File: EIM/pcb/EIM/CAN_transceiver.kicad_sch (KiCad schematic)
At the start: 5 parts, among them U3 SN65HVD233

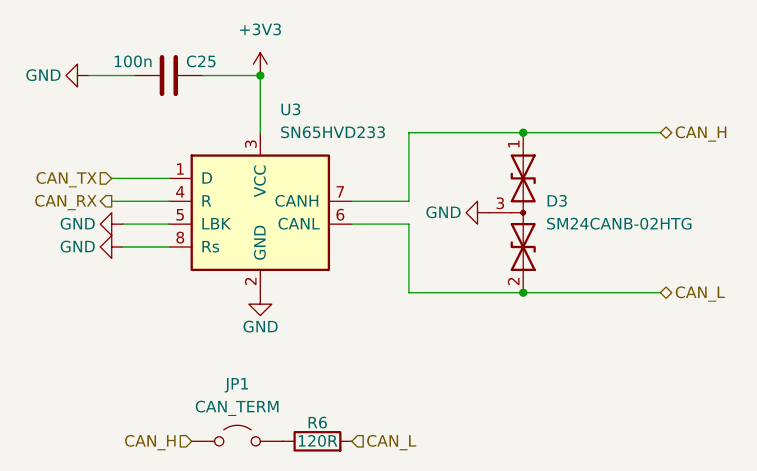
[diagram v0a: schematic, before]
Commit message: added Arjun's comments, assigned some MCU pins
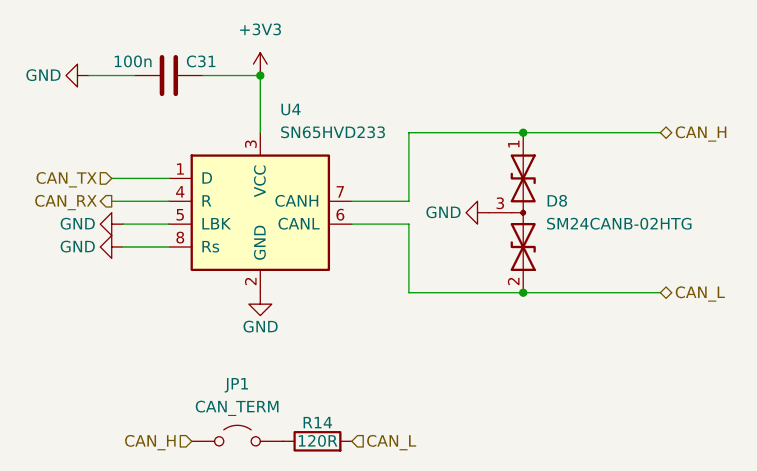
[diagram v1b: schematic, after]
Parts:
- renumbered C25 to C31, D3 to D8, R6 to R14, U3 to U4
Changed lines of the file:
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@@
 		(dnp no)
 		(fields_autoplaced yes)
-		(property "Reference" "#PWR034"
+		(property "Reference" "#PWR071"
 			(at 146.05 83.82 0)
 			(effects
@@
 			(project "EIM"
 				(path "/2e0b3b3d-5537-41dc-9fad-4fb33afdbfad/69c642dd-37c7-4978-9805-ffb4d10279e9"
-					(reference "#PWR034")
-					(unit 1)
-				)
-				(path "/2e0b3b3d-5537-41dc-9fad-4fb33afdbfad/adcbb2f8-dbde-4949-a46c-bc524f70d203"
-					(reference "#PWR041")
+					(reference "#PWR071")
+					(unit 1)
+				)
+				(path "/2e0b3b3d-5537-41dc-9fad-4fb33afdbfad/adcbb2f8-dbde-4949-a46c-bc524f70d203"
+					(reference "#PWR077")
 					(unit 1)
 				)
@@
 		(on_board yes)
 		(dnp no)
-		(property "Reference" "R6"
+		(property "Reference" "R14"
 			(at 152.4 118.618 90)
 			(effects
@@
 			(project "EIM"
 				(path "/2e0b3b3d-5537-41dc-9fad-4fb33afdbfad/69c642dd-37c7-4978-9805-ffb4d10279e9"
-					(reference "R6")
-					(unit 1)
-				)
-				(path "/2e0b3b3d-5537-41dc-9fad-4fb33afdbfad/adcbb2f8-dbde-4949-a46c-bc524f70d203"
-					(reference "R7")
+					(reference "R14")
+					(unit 1)
+				)
+				(path "/2e0b3b3d-5537-41dc-9fad-4fb33afdbfad/adcbb2f8-dbde-4949-a46c-bc524f70d203"
+					(reference "R15")
 					(unit 1)
 				)
@@
 		(on_board yes)
 		(dnp no)
-		(property "Reference" "#PWR048"
+		(property "Reference" "#PWR073"
 			(at 165.1 95.25 0)
 			(effects
@@
 			(project "EIM"
 				(path "/2e0b3b3d-5537-41dc-9fad-4fb33afdbfad/69c642dd-37c7-4978-9805-ffb4d10279e9"
-					(reference "#PWR048")
-					(unit 1)
-				)
-				(path "/2e0b3b3d-5537-41dc-9fad-4fb33afdbfad/adcbb2f8-dbde-4949-a46c-bc524f70d203"
-					(reference "#PWR049")
+					(reference "#PWR073")
+					(unit 1)
+				)
+				(path "/2e0b3b3d-5537-41dc-9fad-4fb33afdbfad/adcbb2f8-dbde-4949-a46c-bc524f70d203"
+					(reference "#PWR079")
 					(unit 1)
 				)
@@
 		(dnp no)
 		(fields_autoplaced yes)
-		(property "Reference" "D3"
+		(property "Reference" "D8"
 			(at 177.8 93.9799 90)
 			(effects
@@
 			(project "EIM"
 				(path "/2e0b3b3d-5537-41dc-9fad-4fb33afdbfad/69c642dd-37c7-4978-9805-ffb4d10279e9"
-					(reference "D3")
-					(unit 1)
-				)
-				(path "/2e0b3b3d-5537-41dc-9fad-4fb33afdbfad/adcbb2f8-dbde-4949-a46c-bc524f70d203"
-					(reference "D4")
+					(reference "D8")
+					(unit 1)
+				)
+				(path "/2e0b3b3d-5537-41dc-9fad-4fb33afdbfad/adcbb2f8-dbde-4949-a46c-bc524f70d203"
+					(reference "D9")
 					(unit 1)
 				)
@@
 		(on_board yes)
 		(dnp no)
-		(property "Reference" "C25"
+		(property "Reference" "C31"
 			(at 141.224 78.486 90)
 			(effects
@@
 			(project "EIM"
 				(path "/2e0b3b3d-5537-41dc-9fad-4fb33afdbfad/69c642dd-37c7-4978-9805-ffb4d10279e9"
-					(reference "C25")
-					(unit 1)
-				)
-				(path "/2e0b3b3d-5537-41dc-9fad-4fb33afdbfad/adcbb2f8-dbde-4949-a46c-bc524f70d203"
-					(reference "C26")
+					(reference "C31")
+					(unit 1)
+				)
+				(path "/2e0b3b3d-5537-41dc-9fad-4fb33afdbfad/adcbb2f8-dbde-4949-a46c-bc524f70d203"
+					(reference "C32")
 					(unit 1)
 				)
@@
 		(on_board yes)
 		(dnp no)
-		(property "Reference" "#PWR035"
+		(property "Reference" "#PWR072"
 			(at 146.05 110.49 0)
 			(effects
@@
 			(project "EIM"
 				(path "/2e0b3b3d-5537-41dc-9fad-4fb33afdbfad/69c642dd-37c7-4978-9805-ffb4d10279e9"
-					(reference "#PWR035")
-					(unit 1)
-				)
-				(path "/2e0b3b3d-5537-41dc-9fad-4fb33afdbfad/adcbb2f8-dbde-4949-a46c-bc524f70d203"
-					(reference "#PWR042")
+					(reference "#PWR072")
+					(unit 1)
+				)
+				(path "/2e0b3b3d-5537-41dc-9fad-4fb33afdbfad/adcbb2f8-dbde-4949-a46c-bc524f70d203"
+					(reference "#PWR078")
 					(unit 1)
 				)
@@
 		(on_board yes)
 		(dnp no)
-		(property "Reference" "#PWR036"
+		(property "Reference" "#PWR069"
 			(at 124.46 96.52 0)
 			(effects
@@
 			(project "EIM"
 				(path "/2e0b3b3d-5537-41dc-9fad-4fb33afdbfad/69c642dd-37c7-4978-9805-ffb4d10279e9"
-					(reference "#PWR036")
-					(unit 1)
-				)
-				(path "/2e0b3b3d-5537-41dc-9fad-4fb33afdbfad/adcbb2f8-dbde-4949-a46c-bc524f70d203"
-					(reference "#PWR039")
+					(reference "#PWR069")
+					(unit 1)
+				)
+				(path "/2e0b3b3d-5537-41dc-9fad-4fb33afdbfad/adcbb2f8-dbde-4949-a46c-bc524f70d203"
+					(reference "#PWR075")
 					(unit 1)
 				)
@@
 		(on_board yes)
 		(dnp no)
-		(property "Reference" "#PWR037"
+		(property "Reference" "#PWR070"
 			(at 124.46 99.06 0)
 			(effects
@@
 			(project "EIM"
 				(path "/2e0b3b3d-5537-41dc-9fad-4fb33afdbfad/69c642dd-37c7-4978-9805-ffb4d10279e9"
-					(reference "#PWR037")
-					(unit 1)
-				)
-				(path "/2e0b3b3d-5537-41dc-9fad-4fb33afdbfad/adcbb2f8-dbde-4949-a46c-bc524f70d203"
-					(reference "#PWR040")
+					(reference "#PWR070")
+					(unit 1)
+				)
+				(path "/2e0b3b3d-5537-41dc-9fad-4fb33afdbfad/adcbb2f8-dbde-4949-a46c-bc524f70d203"
+					(reference "#PWR076")
 					(unit 1)
 				)
@@
 		(on_board yes)
 		(dnp no)
-		(property "Reference" "#PWR033"
+		(property "Reference" "#PWR068"
 			(at 120.65 80.01 0)
 			(effects
@@
 			(project "EIM"
 				(path "/2e0b3b3d-5537-41dc-9fad-4fb33afdbfad/69c642dd-37c7-4978-9805-ffb4d10279e9"
-					(reference "#PWR033")
-					(unit 1)
-				)
-				(path "/2e0b3b3d-5537-41dc-9fad-4fb33afdbfad/adcbb2f8-dbde-4949-a46c-bc524f70d203"
-					(reference "#PWR038")
+					(reference "#PWR068")
+					(unit 1)
+				)
+				(path "/2e0b3b3d-5537-41dc-9fad-4fb33afdbfad/adcbb2f8-dbde-4949-a46c-bc524f70d203"
+					(reference "#PWR074")
 					(unit 1)
 				)
@@
 		(dnp no)
 		(fields_autoplaced yes)
-		(property "Reference" "U3"
+		(property "Reference" "U4"
 			(at 148.2441 83.82 0)
 			(effects
@@
 			(project "EIM"
 				(path "/2e0b3b3d-5537-41dc-9fad-4fb33afdbfad/69c642dd-37c7-4978-9805-ffb4d10279e9"
-					(reference "U3")
-					(unit 1)
-				)
-				(path "/2e0b3b3d-5537-41dc-9fad-4fb33afdbfad/adcbb2f8-dbde-4949-a46c-bc524f70d203"
 					(reference "U4")
 					(unit 1)
 				)
+				(path "/2e0b3b3d-5537-41dc-9fad-4fb33afdbfad/adcbb2f8-dbde-4949-a46c-bc524f70d203"
+					(reference "U5")
+					(unit 1)
+				)

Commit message: Layout 75% done, before 8V bus deletion
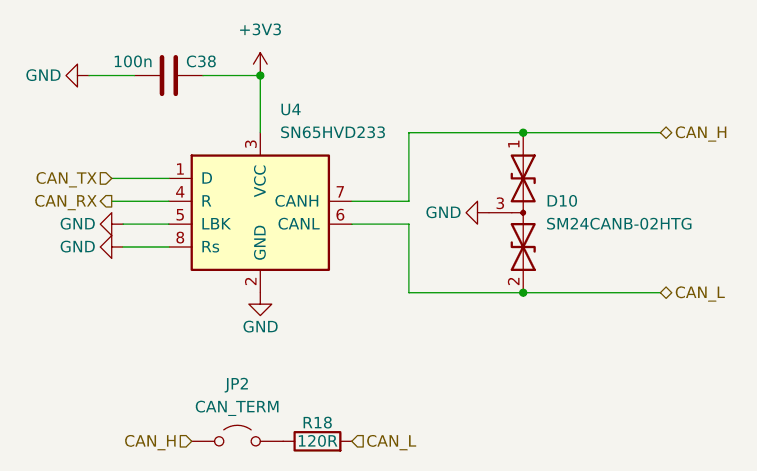
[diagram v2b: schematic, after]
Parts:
- renumbered C31 to C38, D8 to D10, JP1 to JP2, R14 to R18
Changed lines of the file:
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@@
 		(dnp no)
 		(fields_autoplaced yes)
-		(property "Reference" "#PWR071"
+		(property "Reference" "#PWR080"
 			(at 146.05 83.82 0)
 			(effects
@@
 			(project "EIM"
 				(path "/2e0b3b3d-5537-41dc-9fad-4fb33afdbfad/69c642dd-37c7-4978-9805-ffb4d10279e9"
-					(reference "#PWR071")
-					(unit 1)
-				)
-				(path "/2e0b3b3d-5537-41dc-9fad-4fb33afdbfad/adcbb2f8-dbde-4949-a46c-bc524f70d203"
-					(reference "#PWR077")
+					(reference "#PWR080")
+					(unit 1)
+				)
+				(path "/2e0b3b3d-5537-41dc-9fad-4fb33afdbfad/adcbb2f8-dbde-4949-a46c-bc524f70d203"
+					(reference "#PWR086")
 					(unit 1)
 				)
@@
 		(dnp no)
 		(fields_autoplaced yes)
-		(property "Reference" "JP1"
+		(property "Reference" "JP2"
 			(at 143.51 114.3 0)
 			(effects
@@
 			(project "EIM"
 				(path "/2e0b3b3d-5537-41dc-9fad-4fb33afdbfad/69c642dd-37c7-4978-9805-ffb4d10279e9"
-					(reference "JP1")
-					(unit 1)
-				)
-				(path "/2e0b3b3d-5537-41dc-9fad-4fb33afdbfad/adcbb2f8-dbde-4949-a46c-bc524f70d203"
 					(reference "JP2")
+					(unit 1)
+				)
+				(path "/2e0b3b3d-5537-41dc-9fad-4fb33afdbfad/adcbb2f8-dbde-4949-a46c-bc524f70d203"
+					(reference "JP3")
 					(unit 1)
 				)
@@
 		(on_board yes)
 		(dnp no)
-		(property "Reference" "R14"
+		(property "Reference" "R18"
 			(at 152.4 118.618 90)
 			(effects
@@
 			(project "EIM"
 				(path "/2e0b3b3d-5537-41dc-9fad-4fb33afdbfad/69c642dd-37c7-4978-9805-ffb4d10279e9"
-					(reference "R14")
-					(unit 1)
-				)
-				(path "/2e0b3b3d-5537-41dc-9fad-4fb33afdbfad/adcbb2f8-dbde-4949-a46c-bc524f70d203"
-					(reference "R15")
+					(reference "R18")
+					(unit 1)
+				)
+				(path "/2e0b3b3d-5537-41dc-9fad-4fb33afdbfad/adcbb2f8-dbde-4949-a46c-bc524f70d203"
+					(reference "R19")
 					(unit 1)
 				)
@@
 		(on_board yes)
 		(dnp no)
-		(property "Reference" "#PWR073"
+		(property "Reference" "#PWR082"
 			(at 165.1 95.25 0)
 			(effects
@@
 			(project "EIM"
 				(path "/2e0b3b3d-5537-41dc-9fad-4fb33afdbfad/69c642dd-37c7-4978-9805-ffb4d10279e9"
-					(reference "#PWR073")
-					(unit 1)
-				)
-				(path "/2e0b3b3d-5537-41dc-9fad-4fb33afdbfad/adcbb2f8-dbde-4949-a46c-bc524f70d203"
-					(reference "#PWR079")
+					(reference "#PWR082")
+					(unit 1)
+				)
+				(path "/2e0b3b3d-5537-41dc-9fad-4fb33afdbfad/adcbb2f8-dbde-4949-a46c-bc524f70d203"
+					(reference "#PWR088")
 					(unit 1)
 				)
@@
 		(dnp no)
 		(fields_autoplaced yes)
-		(property "Reference" "D8"
+		(property "Reference" "D10"
 			(at 177.8 93.9799 90)
 			(effects
@@
 			(project "EIM"
 				(path "/2e0b3b3d-5537-41dc-9fad-4fb33afdbfad/69c642dd-37c7-4978-9805-ffb4d10279e9"
-					(reference "D8")
-					(unit 1)
-				)
-				(path "/2e0b3b3d-5537-41dc-9fad-4fb33afdbfad/adcbb2f8-dbde-4949-a46c-bc524f70d203"
-					(reference "D9")
+					(reference "D10")
+					(unit 1)
+				)
+				(path "/2e0b3b3d-5537-41dc-9fad-4fb33afdbfad/adcbb2f8-dbde-4949-a46c-bc524f70d203"
+					(reference "D11")
 					(unit 1)
 				)
@@
 		(on_board yes)
 		(dnp no)
-		(property "Reference" "C31"
+		(property "Reference" "C38"
 			(at 141.224 78.486 90)
 			(effects
@@
 			(project "EIM"
 				(path "/2e0b3b3d-5537-41dc-9fad-4fb33afdbfad/69c642dd-37c7-4978-9805-ffb4d10279e9"
-					(reference "C31")
-					(unit 1)
-				)
-				(path "/2e0b3b3d-5537-41dc-9fad-4fb33afdbfad/adcbb2f8-dbde-4949-a46c-bc524f70d203"
-					(reference "C32")
+					(reference "C38")
+					(unit 1)
+				)
+				(path "/2e0b3b3d-5537-41dc-9fad-4fb33afdbfad/adcbb2f8-dbde-4949-a46c-bc524f70d203"
+					(reference "C39")
 					(unit 1)
 				)
@@
 		(on_board yes)
 		(dnp no)
-		(property "Reference" "#PWR072"
+		(property "Reference" "#PWR081"
 			(at 146.05 110.49 0)
 			(effects
@@
 			(project "EIM"
 				(path "/2e0b3b3d-5537-41dc-9fad-4fb33afdbfad/69c642dd-37c7-4978-9805-ffb4d10279e9"
-					(reference "#PWR072")
-					(unit 1)
-				)
-				(path "/2e0b3b3d-5537-41dc-9fad-4fb33afdbfad/adcbb2f8-dbde-4949-a46c-bc524f70d203"
-					(reference "#PWR078")
+					(reference "#PWR081")
+					(unit 1)
+				)
+				(path "/2e0b3b3d-5537-41dc-9fad-4fb33afdbfad/adcbb2f8-dbde-4949-a46c-bc524f70d203"
+					(reference "#PWR087")
 					(unit 1)
 				)
@@
 		(on_board yes)
 		(dnp no)
-		(property "Reference" "#PWR069"
+		(property "Reference" "#PWR078"
 			(at 124.46 96.52 0)
 			(effects
@@
 			(project "EIM"
 				(path "/2e0b3b3d-5537-41dc-9fad-4fb33afdbfad/69c642dd-37c7-4978-9805-ffb4d10279e9"
-					(reference "#PWR069")
-					(unit 1)
-				)
-				(path "/2e0b3b3d-5537-41dc-9fad-4fb33afdbfad/adcbb2f8-dbde-4949-a46c-bc524f70d203"
-					(reference "#PWR075")
+					(reference "#PWR078")
+					(unit 1)
+				)
+				(path "/2e0b3b3d-5537-41dc-9fad-4fb33afdbfad/adcbb2f8-dbde-4949-a46c-bc524f70d203"
+					(reference "#PWR084")
 					(unit 1)
 				)
@@
 		(on_board yes)
 		(dnp no)
-		(property "Reference" "#PWR070"
+		(property "Reference" "#PWR079"
 			(at 124.46 99.06 0)
 			(effects
@@
 			(project "EIM"
 				(path "/2e0b3b3d-5537-41dc-9fad-4fb33afdbfad/69c642dd-37c7-4978-9805-ffb4d10279e9"
-					(reference "#PWR070")
-					(unit 1)
-				)
-				(path "/2e0b3b3d-5537-41dc-9fad-4fb33afdbfad/adcbb2f8-dbde-4949-a46c-bc524f70d203"
-					(reference "#PWR076")
+					(reference "#PWR079")
+					(unit 1)
+				)
+				(path "/2e0b3b3d-5537-41dc-9fad-4fb33afdbfad/adcbb2f8-dbde-4949-a46c-bc524f70d203"
+					(reference "#PWR085")
 					(unit 1)
 				)
@@
 		(on_board yes)
 		(dnp no)
-		(property "Reference" "#PWR068"
+		(property "Reference" "#PWR077"
 			(at 120.65 80.01 0)
 			(effects
@@
 			(project "EIM"
 				(path "/2e0b3b3d-5537-41dc-9fad-4fb33afdbfad/69c642dd-37c7-4978-9805-ffb4d10279e9"
-					(reference "#PWR068")
-					(unit 1)
-				)
-				(path "/2e0b3b3d-5537-41dc-9fad-4fb33afdbfad/adcbb2f8-dbde-4949-a46c-bc524f70d203"
-					(reference "#PWR074")
-					(unit 1)
-				)
+					(reference "#PWR077")
+					(unit 1)
+				)
+				(path "/2e0b3b3d-5537-41dc-9fad-4fb33afdbfad/adcbb2f8-dbde-4949-a46c-bc524f70d203"
+					(reference "#PWR083")
+					(unit 1)
+				)

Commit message: All components placed and pins assigned.
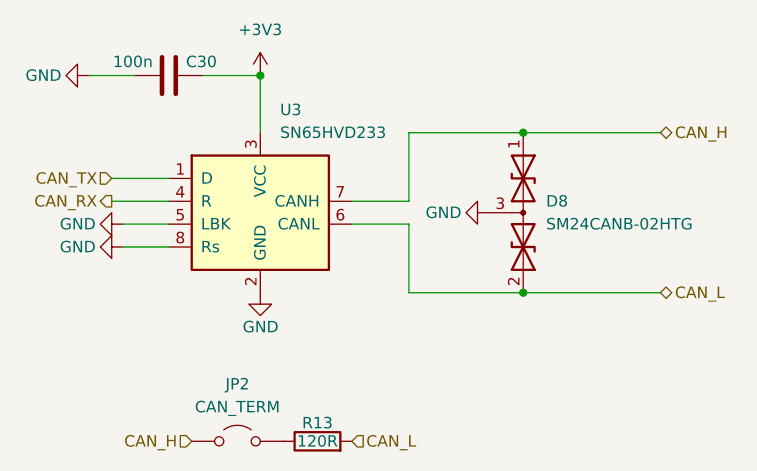
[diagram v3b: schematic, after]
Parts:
- renumbered C38 to C30, D10 to D8, R18 to R13, U4 to U3
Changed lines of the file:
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@@
 		(dnp no)
 		(fields_autoplaced yes)
-		(property "Reference" "#PWR080"
+		(property "Reference" "#PWR073"
 			(at 146.05 83.82 0)
 			(effects
@@
 			(project "EIM"
 				(path "/2e0b3b3d-5537-41dc-9fad-4fb33afdbfad/69c642dd-37c7-4978-9805-ffb4d10279e9"
-					(reference "#PWR080")
-					(unit 1)
-				)
-				(path "/2e0b3b3d-5537-41dc-9fad-4fb33afdbfad/adcbb2f8-dbde-4949-a46c-bc524f70d203"
-					(reference "#PWR086")
+					(reference "#PWR073")
+					(unit 1)
+				)
+				(path "/2e0b3b3d-5537-41dc-9fad-4fb33afdbfad/adcbb2f8-dbde-4949-a46c-bc524f70d203"
+					(reference "#PWR079")
 					(unit 1)
 				)
@@
 		(on_board yes)
 		(dnp no)
-		(property "Reference" "R18"
+		(property "Reference" "R13"
 			(at 152.4 118.618 90)
 			(effects
@@
 			(project "EIM"
 				(path "/2e0b3b3d-5537-41dc-9fad-4fb33afdbfad/69c642dd-37c7-4978-9805-ffb4d10279e9"
-					(reference "R18")
-					(unit 1)
-				)
-				(path "/2e0b3b3d-5537-41dc-9fad-4fb33afdbfad/adcbb2f8-dbde-4949-a46c-bc524f70d203"
-					(reference "R19")
+					(reference "R13")
+					(unit 1)
+				)
+				(path "/2e0b3b3d-5537-41dc-9fad-4fb33afdbfad/adcbb2f8-dbde-4949-a46c-bc524f70d203"
+					(reference "R14")
 					(unit 1)
 				)
@@
 		(on_board yes)
 		(dnp no)
-		(property "Reference" "#PWR082"
+		(property "Reference" "#PWR075"
 			(at 165.1 95.25 0)
 			(effects
@@
 			(project "EIM"
 				(path "/2e0b3b3d-5537-41dc-9fad-4fb33afdbfad/69c642dd-37c7-4978-9805-ffb4d10279e9"
-					(reference "#PWR082")
-					(unit 1)
-				)
-				(path "/2e0b3b3d-5537-41dc-9fad-4fb33afdbfad/adcbb2f8-dbde-4949-a46c-bc524f70d203"
-					(reference "#PWR088")
+					(reference "#PWR075")
+					(unit 1)
+				)
+				(path "/2e0b3b3d-5537-41dc-9fad-4fb33afdbfad/adcbb2f8-dbde-4949-a46c-bc524f70d203"
+					(reference "#PWR081")
 					(unit 1)
 				)
@@
 		(dnp no)
 		(fields_autoplaced yes)
-		(property "Reference" "D10"
+		(property "Reference" "D8"
 			(at 177.8 93.9799 90)
 			(effects
@@
 			(project "EIM"
 				(path "/2e0b3b3d-5537-41dc-9fad-4fb33afdbfad/69c642dd-37c7-4978-9805-ffb4d10279e9"
-					(reference "D10")
-					(unit 1)
-				)
-				(path "/2e0b3b3d-5537-41dc-9fad-4fb33afdbfad/adcbb2f8-dbde-4949-a46c-bc524f70d203"
-					(reference "D11")
+					(reference "D8")
+					(unit 1)
+				)
+				(path "/2e0b3b3d-5537-41dc-9fad-4fb33afdbfad/adcbb2f8-dbde-4949-a46c-bc524f70d203"
+					(reference "D9")
 					(unit 1)
 				)
@@
 		(on_board yes)
 		(dnp no)
-		(property "Reference" "C38"
+		(property "Reference" "C30"
 			(at 141.224 78.486 90)
 			(effects
@@
 			(project "EIM"
 				(path "/2e0b3b3d-5537-41dc-9fad-4fb33afdbfad/69c642dd-37c7-4978-9805-ffb4d10279e9"
-					(reference "C38")
-					(unit 1)
-				)
-				(path "/2e0b3b3d-5537-41dc-9fad-4fb33afdbfad/adcbb2f8-dbde-4949-a46c-bc524f70d203"
-					(reference "C39")
+					(reference "C30")
+					(unit 1)
+				)
+				(path "/2e0b3b3d-5537-41dc-9fad-4fb33afdbfad/adcbb2f8-dbde-4949-a46c-bc524f70d203"
+					(reference "C31")
 					(unit 1)
 				)
@@
 		(on_board yes)
 		(dnp no)
-		(property "Reference" "#PWR081"
+		(property "Reference" "#PWR074"
 			(at 146.05 110.49 0)
 			(effects
@@
 			(project "EIM"
 				(path "/2e0b3b3d-5537-41dc-9fad-4fb33afdbfad/69c642dd-37c7-4978-9805-ffb4d10279e9"
-					(reference "#PWR081")
-					(unit 1)
-				)
-				(path "/2e0b3b3d-5537-41dc-9fad-4fb33afdbfad/adcbb2f8-dbde-4949-a46c-bc524f70d203"
-					(reference "#PWR087")
+					(reference "#PWR074")
+					(unit 1)
+				)
+				(path "/2e0b3b3d-5537-41dc-9fad-4fb33afdbfad/adcbb2f8-dbde-4949-a46c-bc524f70d203"
+					(reference "#PWR080")
 					(unit 1)
 				)
@@
 		(on_board yes)
 		(dnp no)
-		(property "Reference" "#PWR078"
+		(property "Reference" "#PWR071"
 			(at 124.46 96.52 0)
 			(effects
@@
 			(project "EIM"
 				(path "/2e0b3b3d-5537-41dc-9fad-4fb33afdbfad/69c642dd-37c7-4978-9805-ffb4d10279e9"
-					(reference "#PWR078")
-					(unit 1)
-				)
-				(path "/2e0b3b3d-5537-41dc-9fad-4fb33afdbfad/adcbb2f8-dbde-4949-a46c-bc524f70d203"
-					(reference "#PWR084")
+					(reference "#PWR071")
+					(unit 1)
+				)
+				(path "/2e0b3b3d-5537-41dc-9fad-4fb33afdbfad/adcbb2f8-dbde-4949-a46c-bc524f70d203"
+					(reference "#PWR077")
 					(unit 1)
 				)
@@
 		(on_board yes)
 		(dnp no)
-		(property "Reference" "#PWR079"
+		(property "Reference" "#PWR072"
 			(at 124.46 99.06 0)
 			(effects
@@
 			(project "EIM"
 				(path "/2e0b3b3d-5537-41dc-9fad-4fb33afdbfad/69c642dd-37c7-4978-9805-ffb4d10279e9"
-					(reference "#PWR079")
-					(unit 1)
-				)
-				(path "/2e0b3b3d-5537-41dc-9fad-4fb33afdbfad/adcbb2f8-dbde-4949-a46c-bc524f70d203"
-					(reference "#PWR085")
+					(reference "#PWR072")
+					(unit 1)
+				)
+				(path "/2e0b3b3d-5537-41dc-9fad-4fb33afdbfad/adcbb2f8-dbde-4949-a46c-bc524f70d203"
+					(reference "#PWR078")
 					(unit 1)
 				)
@@
 		(on_board yes)
 		(dnp no)
-		(property "Reference" "#PWR077"
+		(property "Reference" "#PWR070"
 			(at 120.65 80.01 0)
 			(effects
@@
 			(project "EIM"
 				(path "/2e0b3b3d-5537-41dc-9fad-4fb33afdbfad/69c642dd-37c7-4978-9805-ffb4d10279e9"
-					(reference "#PWR077")
-					(unit 1)
-				)
-				(path "/2e0b3b3d-5537-41dc-9fad-4fb33afdbfad/adcbb2f8-dbde-4949-a46c-bc524f70d203"
-					(reference "#PWR083")
+					(reference "#PWR070")
+					(unit 1)
+				)
+				(path "/2e0b3b3d-5537-41dc-9fad-4fb33afdbfad/adcbb2f8-dbde-4949-a46c-bc524f70d203"
+					(reference "#PWR076")
 					(unit 1)
 				)
@@
 		(dnp no)
 		(fields_autoplaced yes)
-		(property "Reference" "U4"
+		(property "Reference" "U3"
 			(at 148.2441 83.82 0)
 			(effects
@@
 			(project "EIM"
 				(path "/2e0b3b3d-5537-41dc-9fad-4fb33afdbfad/69c642dd-37c7-4978-9805-ffb4d10279e9"
+					(reference "U3")
+					(unit 1)
+				)
+				(path "/2e0b3b3d-5537-41dc-9fad-4fb33afdbfad/adcbb2f8-dbde-4949-a46c-bc524f70d203"
 					(reference "U4")
 					(unit 1)
 				)
-				(path "/2e0b3b3d-5537-41dc-9fad-4fb33afdbfad/adcbb2f8-dbde-4949-a46c-bc524f70d203"
-					(reference "U5")
-					(unit 1)
-				)
